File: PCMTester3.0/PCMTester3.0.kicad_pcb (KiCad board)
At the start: 2 copper layers, 150 x 150 mm, 21 parts

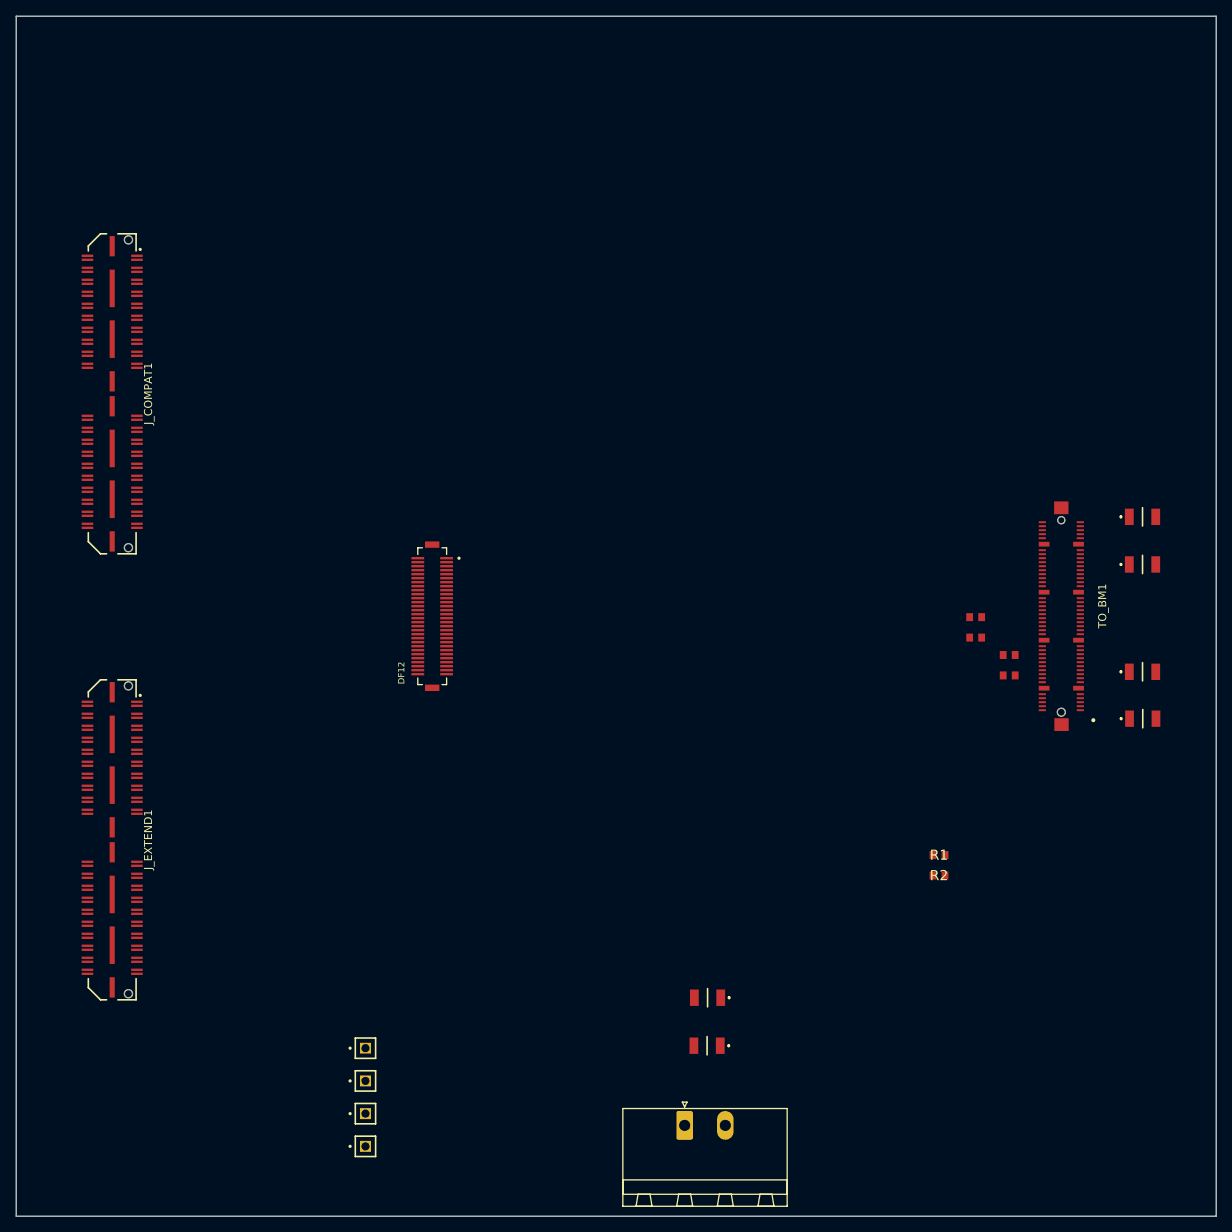
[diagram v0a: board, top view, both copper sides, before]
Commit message: component layout on board
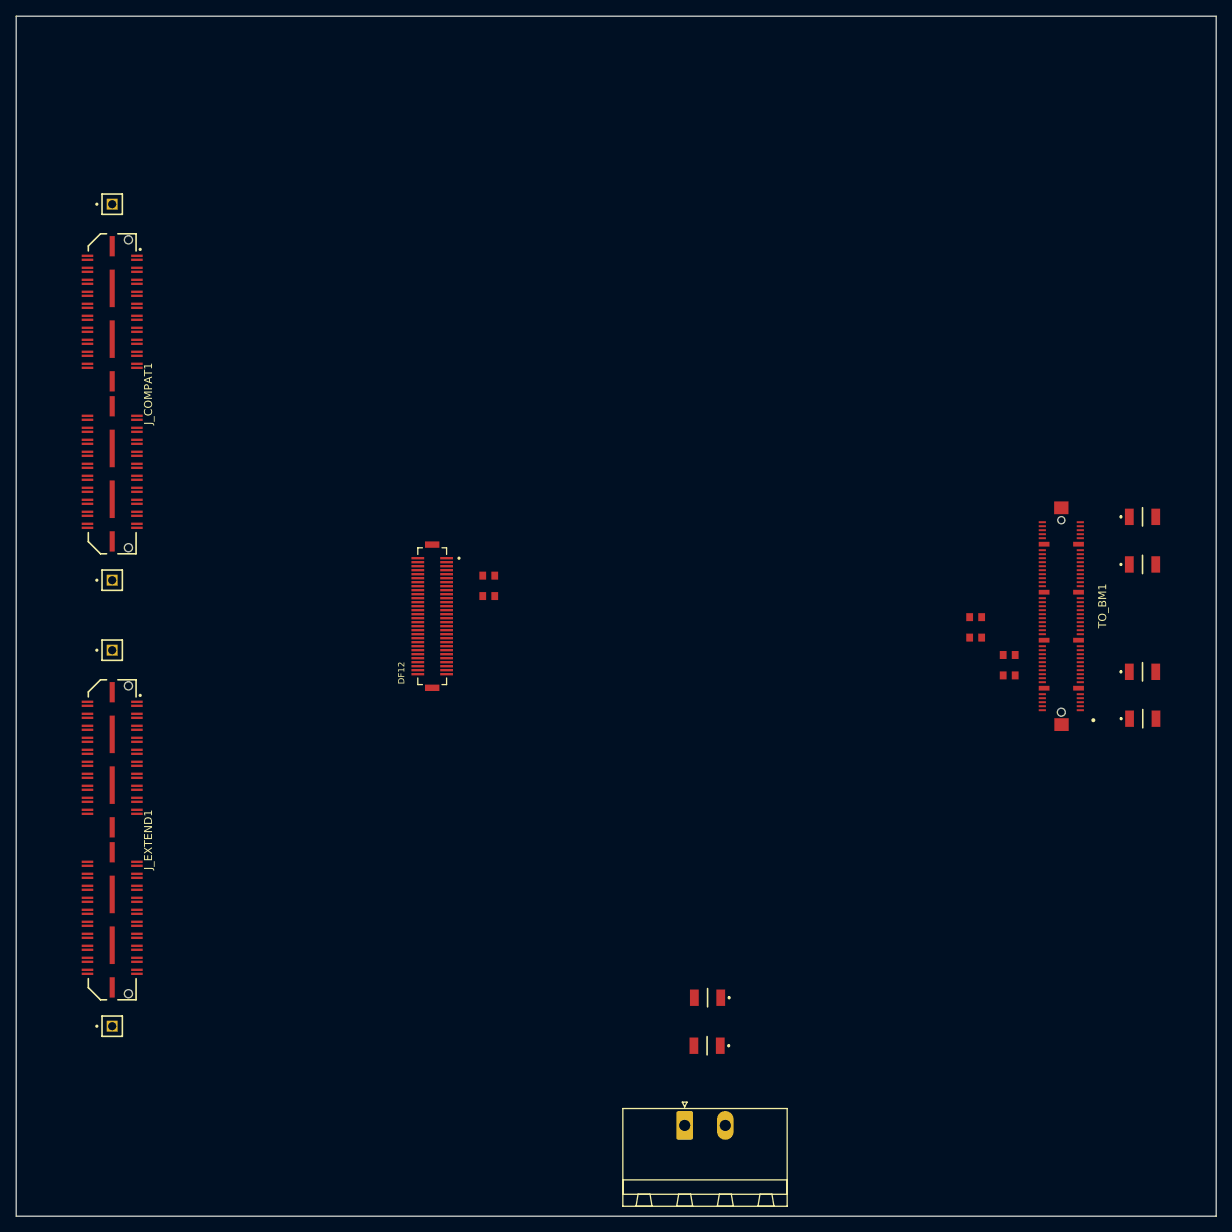
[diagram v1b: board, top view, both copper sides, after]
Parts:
- moved TP1 110.1 mm to (84.2, 37.6)
- moved TP2 70.1 mm to (84.2, 84.6)
- moved R2 67.6 mm to (131.3, 84.1), turned to 180 degrees
- moved TP3 66.0 mm to (84.2, 93.4)
- moved R1 64.9 mm to (131.3, 86.6), turned to 180 degrees
- moved TP_VBRD1 35.0 mm to (84.2, 140.4)

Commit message: added ground and power planes
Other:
- copper layers 2 -> 6
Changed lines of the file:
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@@
 	(layers
 		(0 "F.Cu" signal)
+		(4 "In1.Cu" power "GND.Cu")
+		(6 "In2.Cu" power "VDD.Cu")
+		(8 "In3.Cu" signal)
+		(10 "In4.Cu" signal)
 		(2 "B.Cu" signal)
 		(9 "F.Adhes" user "F.Adhesive")
@@
 	)
 	(setup
+		(stackup
+			(layer "F.SilkS"
+				(type "Top Silk Screen")
+			)
+			(layer "F.Paste"
+				(type "Top Solder Paste")
+			)
+			(layer "F.Mask"
+				(type "Top Solder Mask")
+				(thickness 0.01)
+			)
+			(layer "F.Cu"
+				(type "copper")
+				(thickness 0.035)
+			)
+			(layer "dielectric 1"
+				(type "prepreg")
+				(thickness 0.1)
+				(material "FR4")
+				(epsilon_r 4.5)
+				(loss_tangent 0.02)
+			)
+			(layer "In1.Cu"
+				(type "copper")
+				(thickness 0.035)
+			)
+			(layer "dielectric 2"
+				(type "core")
+				(thickness 0.535)
+				(material "FR4")
+				(epsilon_r 4.5)
+				(loss_tangent 0.02)
+			)
+			(layer "In2.Cu"
+				(type "copper")
+				(thickness 0.035)
+			)
+			(layer "dielectric 3"
+				(type "prepreg")
+				(thickness 0.1)
+				(material "FR4")
+				(epsilon_r 4.5)
+				(loss_tangent 0.02)
+			)
+			(layer "In3.Cu"
+				(type "copper")
+				(thickness 0.035)
+			)
+			(layer "dielectric 4"
+				(type "core")
+				(thickness 0.535)
+				(material "FR4")
+				(epsilon_r 4.5)
+				(loss_tangent 0.02)
+			)
+			(layer "In4.Cu"
+				(type "copper")
+				(thickness 0.035)
+			)
+			(layer "dielectric 5"
+				(type "prepreg")
+				(thickness 0.1)
+				(material "FR4")
+				(epsilon_r 4.5)
+				(loss_tangent 0.02)
+			)
+			(layer "B.Cu"
+				(type "copper")
+				(thickness 0.035)
+			)
+			(layer "B.Mask"
+				(type "Bottom Solder Mask")
+				(thickness 0.01)
+			)
+			(layer "B.Paste"
+				(type "Bottom Solder Paste")
+			)
+			(layer "B.SilkS"
+				(type "Bottom Silk Screen")
+			)
+			(copper_finish "None")
+			(dielectric_constraints no)
+		)
 		(pad_to_mask_clearance 0)
 		(allow_soldermask_bridges_in_footprints no)

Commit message: power plane with jumper and ground plane
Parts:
- added JP1: Jumper_3_Open, Connector_PinHeader_2.54mm:PinHeader_1x03_P2.54mm_Vertical, F.Cu at (127.6, 157.5)
- moved C5 11.3 mm to (158.8, 131.5)
- moved C6 11.3 mm to (158.8, 125.5)
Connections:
- J_COMPAT1 pad 10: /VBRD -> /3V3D
- J_COMPAT1 pad 12: /VBRD -> /3V3D
- J_COMPAT1 pad 14: /VBRD -> /3V3D
- J_COMPAT1 pad 16: /VBRD -> /3V3D
- J_COMPAT1 pad 18: /VBRD -> /3V3D
- J_COMPAT1 pad 20: /VBRD -> /3V3D
- J_COMPAT1 pad 22: /VBRD -> /3V3D
- J_COMPAT1 pad 24: /VBRD -> /3V3D
- J_COMPAT1 pad 26: /VBRD -> /3V3D
- J_COMPAT1 pad 28: /VBRD -> /3V3D
- J_COMPAT1 pad 6: /VBRD -> /3V3D
- J_COMPAT1 pad 8: /VBRD -> /3V3D
- PWR_CORE1 pad 1: VDD -> Net-(JP1-A)
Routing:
- added copper zone on In2.Cu, net /3V3D
- added copper zone on In1.Cu, net GND
- added copper zone on In2.Cu, net Net-(JP1-A)
- added copper zone on In2.Cu, net VDD
